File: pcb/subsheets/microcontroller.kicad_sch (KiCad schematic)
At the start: 2 parts, among them SW1 RESET, U1 Raspberry-Pi-Pico

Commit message: renamed dirs
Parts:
- renumbered SW1 to SW?
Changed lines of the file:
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@@
   (symbol (lib_id "Switch:SW_Push_Dual") (at 67.31 66.04 0) (unit 1)
     (in_bom yes) (on_board yes) (dnp no) (fields_autoplaced)
-    (property "Reference" "SW1" (at 67.31 58.42 0)
+    (property "Reference" "SW?" (at 67.31 58.42 0)
       (effects (font (size 1.27 1.27)))
     )
@@
       (project "belt"
         (path "/33e5c18d-f516-4ab7-aaea-c68685305111"
-          (reference "SW1") (unit 1)
+          (reference "SW?") (unit 1)
         )
         (path "/33e5c18d-f516-4ab7-aaea-c68685305111/0e4903ad-ca28-4f97-b4fc-99c0ae9223e0"

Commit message: fixed everything (ERC is no longer mad)
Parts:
- removed SW?: RESET, symbol Switch:SW_Push_Dual
- added SW?: RESET, symbol Switch:SW_Push_Dual
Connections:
- net +3.3V: no longer U1.35 (ADC_VREF)
- net GND: now also SW?.1, SW?.3; no longer U1.D2 (GND)
- net ~{Reset}: now also U1.37 (3V3_EN), SW?.2, SW?.4; no longer U1.30 (~{RUN})
- net SDA_{0}: now reaches U1.6 (GP_{4})
- net SCL_{0}: now reaches U1.7 (GP_{5})
- net DataBaro renamed V_{ADC0}
- net DataGndRef renamed GNDA
- net DataTemp: no longer names the net of U1.32 (GP_{27})
- no-connect marks 33 -> 25
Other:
- note added: "ADC_{2} is tied to GNDA for ADC offset approximation."
- note added: "To reduce ADC noise and offset, connect an external 3.0V shunt reference (such as LM4040) from ADC_V_{REF} to GNDA."
- note removed: "+3.3V net is otherwise unused"

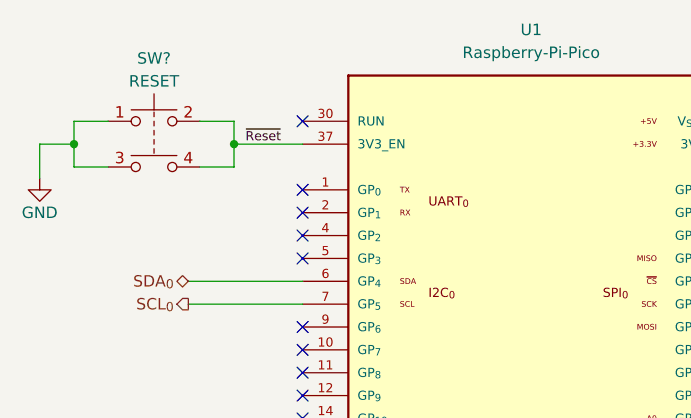
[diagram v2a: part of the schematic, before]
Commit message: fixed all the resistors
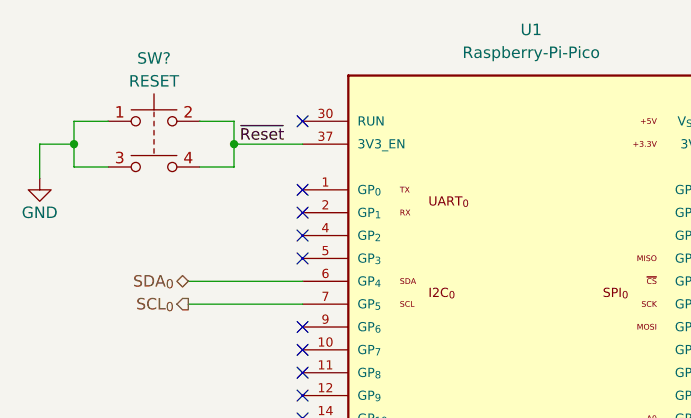
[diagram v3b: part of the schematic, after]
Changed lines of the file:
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@@
     (effects (font (size 0.635 0.635) bold) (justify left bottom))
   )
-  (label "~{Reset}" (at 90.17 71.12 0) (fields_autoplaced)
-    (effects (font (size 1.016 1.016)) (justify left bottom))
+  (label "~{Reset}" (at 89.535 71.12 0) (fields_autoplaced)
+    (effects (font (size 1.27 1.27)) (justify left bottom))
   )
   (hierarchical_label "SCL_{0}" (shape output) (at 83.82 88.9 180) (fields_autoplaced)

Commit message: mostly finished schematic
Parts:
- added D1: Power-GRN, symbol Device:LED
- added D2: Reset-RED, symbol Device:LED
- added R5, R6: 1K, symbol Device:R
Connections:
- net +3.3V: now also D2.2 (A)
- net +5V: now also D1.2 (A)
- net GND: now also R5.2, R6.2
- new net: D1.1 (K), R5.1
- new net: D2.1 (K), R6.1
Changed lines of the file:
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@@
   (title_block
     (title "BELT Microcontroller")
-    (date "2023-12-31")
+    (date "2024-01-02")
     (rev "0.2")
     (company "Rice Eclipse")
@@
     (stroke (width 0) (type default))
   )
+  (wire (pts (xy 227.33 97.79) (xy 227.33 100.33))
+    (stroke (width 0) (type default))
+  )
+  (wire (pts (xy 208.28 77.47) (xy 208.28 80.01))
+    (stroke (width 0) (type default))
+  )
   (wire (pts (xy 158.75 121.92) (xy 158.75 125.73))
     (stroke (width 0) (type default))
   )
+  (wire (pts (xy 227.33 77.47) (xy 227.33 80.01))
+    (stroke (width 0) (type default))
+  )
   (wire (pts (xy 83.82 86.36) (xy 96.52 86.36))
     (stroke (width 0) (type default))
   )
+  (wire (pts (xy 208.28 97.79) (xy 208.28 100.33))
+    (stroke (width 0) (type default))
+  )
   (wire (pts (xy 67.31 71.12) (xy 71.12 71.12))
     (stroke (width 0) (type default))
@@
     (stroke (width 0) (type default))
   )
+  (wire (pts (xy 227.33 87.63) (xy 227.33 90.17))
+    (stroke (width 0) (type default))
+  )
   (wire (pts (xy 71.12 68.58) (xy 71.12 71.12))
     (stroke (width 0) (type default))
@@
     (stroke (width 0) (type default))
   )
+  (wire (pts (xy 208.28 87.63) (xy 208.28 90.17))
+    (stroke (width 0) (type default))
+  )
   (wire (pts (xy 158.75 67.31) (xy 158.75 71.12))
     (stroke (width 0) (type default))
@@
   (wire (pts (xy 67.31 74.93) (xy 67.31 71.12))
     (stroke (width 0) (type default))
+  )
+  (text_box "Indicator LEDs"
+    (at 203.2 63.5 0) (size 39.37 44.45)
+    (stroke (width 0.254) (type solid) (color 0 0 0 1))
+    (fill (type none))
+    (effects (font (size 2.794 2.794) (thickness 0.5588) bold (color 0 0 0 1)) (justify left top))
   )
   (text "ADC_{2} is tied to GNDA for\nADC offset approximation."
@@
     (effects (font (size 1.27 1.27)) (justify left))
   )
+  (symbol (lib_id "Device:LED") (at 208.28 83.82 90) (unit 1)
+    (in_bom yes) (on_board yes) (dnp no)
+    (property "Reference" "D1" (at 210.82 82.55 90)
+      (effects (font (size 1.27 1.27)) (justify right))
+    )
+    (property "Value" "Power-GRN" (at 210.82 85.09 90)
+      (effects (font (size 1.27 1.27)) (justify right))
+    )
+    (property "Footprint" "" (at 208.28 83.82 0)
+      (effects (font (size 1.27 1.27)) hide)
+    )
+    (property "Datasheet" "~" (at 208.28 83.82 0)
+      (effects (font (size 1.27 1.27)) hide)
+    )
+    (pin "1")
+    (pin "2")
+    (instances
+      (project "belt"
+        (path "/33e5c18d-f516-4ab7-aaea-c68685305111"
+          (reference "D1") (unit 1)
+        )
+        (path "/33e5c18d-f516-4ab7-aaea-c68685305111/0e4903ad-ca28-4f97-b4fc-99c0ae9223e0"
+          (reference "D1") (unit 1)
+        )
+      )
+    )
+  )
+  (symbol (lib_id "Device:R") (at 227.33 93.98 0) (unit 1)
+    (in_bom yes) (on_board yes) (dnp no)
+    (property "Reference" "R6" (at 229.87 92.71 0)
+      (effects (font (size 1.27 1.27)) (justify left))
+    )
+    (property "Value" "1K" (at 229.87 95.25 0)
+      (effects (font (size 1.27 1.27)) (justify left))
+    )
+    (property "Footprint" "" (at 225.552 93.98 90)
+      (effects (font (size 1.27 1.27)) hide)
+    )
+    (property "Datasheet" "~" (at 227.33 93.98 0)
+      (effects (font (size 1.27 1.27)) hide)
+    )
+    (pin "1")
+    (pin "2")
+    (instances
+      (project "belt"
+        (path "/33e5c18d-f516-4ab7-aaea-c68685305111"
+          (reference "R6") (unit 1)
+        )
+        (path "/33e5c18d-f516-4ab7-aaea-c68685305111/0e4903ad-ca28-4f97-b4fc-99c0ae9223e0"
+          (reference "R6") (unit 1)
+        )
+      )
+    )
+  )
   (symbol (lib_id "power:GNDA") (at 154.94 110.49 0) (unit 1)
     (in_bom yes) (on_board yes) (dnp no)
@@
         (path "/33e5c18d-f516-4ab7-aaea-c68685305111/0e4903ad-ca28-4f97-b4fc-99c0ae9223e0"
           (reference "#PWR05") (unit 1)
+        )
+      )
+    )
+  )
+  (symbol (lib_id "power:GND") (at 227.33 100.33 0) (unit 1)
+    (in_bom yes) (on_board yes) (dnp no)
+    (property "Reference" "#PWR019" (at 227.33 106.68 0)
+      (effects (font (size 1.27 1.27)) hide)
+    )
+    (property "Value" "GND" (at 227.33 104.14 0)
+      (effects (font (size 1.27 1.27)))
+    )
+    (property "Footprint" "" (at 227.33 100.33 0)
+      (effects (font (size 1.27 1.27)) hide)
+    )
+    (property "Datasheet" "" (at 227.33 100.33 0)
+      (effects (font (size 1.27 1.27)) hide)
+    )
+    (pin "1")
+    (instances
+      (project "belt"
+        (path "/33e5c18d-f516-4ab7-aaea-c68685305111"
+          (reference "#PWR019") (unit 1)
+        )
+        (path "/33e5c18d-f516-4ab7-aaea-c68685305111/0e4903ad-ca28-4f97-b4fc-99c0ae9223e0"
+          (reference "#PWR019") (unit 1)
         )
       )
@@
     )
   )
+  (symbol (lib_id "power:+3.3V") (at 227.33 77.47 0) (unit 1)
+    (in_bom yes) (on_board yes) (dnp no)
+    (property "Reference" "#PWR018" (at 227.33 81.28 0)
+      (effects (font (size 1.27 1.27)) hide)
+    )
+    (property "Value" "+3.3V" (at 227.33 73.66 0)
+      (effects (font (size 1.27 1.27)))
+    )
+    (property "Footprint" "" (at 227.33 77.47 0)
+      (effects (font (size 1.27 1.27)) hide)
+    )
+    (property "Datasheet" "" (at 227.33 77.47 0)
+      (effects (font (size 1.27 1.27)) hide)
+    )
+    (pin "1")
+    (instances
+      (project "belt"
+        (path "/33e5c18d-f516-4ab7-aaea-c68685305111"
+          (reference "#PWR018") (unit 1)
+        )
+        (path "/33e5c18d-f516-4ab7-aaea-c68685305111/0e4903ad-ca28-4f97-b4fc-99c0ae9223e0"
+          (reference "#PWR018") (unit 1)
+        )
+      )
+    )
+  )
   (symbol (lib_id "Switch:SW_Push_Dual") (at 80.01 68.58 0) (unit 1)
     (in_bom yes) (on_board yes) (dnp no)
@@
         )
       )
+    )
+  )
+  (symbol (lib_id "Device:R") (at 208.28 93.98 0) (unit 1)
+    (in_bom yes) (on_board yes) (dnp no)
+    (property "Reference" "R5" (at 210.82 92.71 0)
+      (effects (font (size 1.27 1.27)) (justify left))
+    )
+    (property "Value" "1K" (at 210.82 95.25 0)
+      (effects (font (size 1.27 1.27)) (justify left))
+    )
+    (property "Footprint" "" (at 206.502 93.98 90)
+      (effects (font (size 1.27 1.27)) hide)
+    )
+    (property "Datasheet" "~" (at 208.28 93.98 0)
+      (effects (font (size 1.27 1.27)) hide)
+    )
+    (pin "1")
+    (pin "2")
+    (instances
+      (project "belt"
+        (path "/33e5c18d-f516-4ab7-aaea-c68685305111"
+          (reference "R5") (unit 1)
+        )
+        (path "/33e5c18d-f516-4ab7-aaea-c68685305111/0e4903ad-ca28-4f97-b4fc-99c0ae9223e0"
+          (reference "R5") (unit 1)
+        )
+      )
+    )
+  )
+  (symbol (lib_id "power:+5V") (at 208.28 77.47 0) (unit 1)
+    (in_bom yes) (on_board yes) (dnp no)
+    (property "Reference" "#PWR016" (at 208.28 81.28 0)
+      (effects (font (size 1.27 1.27)) hide)
+    )
+    (property "Value" "+5V" (at 208.28 73.66 0)
+      (effects (font (size 1.27 1.27)))
+    )
+    (property "Footprint" "" (at 208.28 77.47 0)
+      (effects (font (size 1.27 1.27)) hide)
+    )
+    (property "Datasheet" "" (at 208.28 77.47 0)
+      (effects (font (size 1.27 1.27)) hide)
+    )
+    (pin "1")
+    (instances
+      (project "belt"
+        (path "/33e5c18d-f516-4ab7-aaea-c68685305111"
+          (reference "#PWR016") (unit 1)
+        )
+        (path "/33e5c18d-f516-4ab7-aaea-c68685305111/0e4903ad-ca28-4f97-b4fc-99c0ae9223e0"
+          (reference "#PWR016") (unit 1)
+        )
+      )
+    )
+  )
+  (symbol (lib_id "power:GND") (at 208.28 100.33 0) (unit 1)
+    (in_bom yes) (on_board yes) (dnp no)
+    (property "Reference" "#PWR017" (at 208.28 106.68 0)
+      (effects (font (size 1.27 1.27)) hide)
+    )
+    (property "Value" "GND" (at 208.28 104.14 0)
+      (effects (font (size 1.27 1.27)))
+    )
+    (property "Footprint" "" (at 208.28 100.33 0)
+      (effects (font (size 1.27 1.27)) hide)
+    )
+    (property "Datasheet" "" (at 208.28 100.33 0)
+      (effects (font (size 1.27 1.27)) hide)
+    )
+    (pin "1")
+    (instances
+      (project "belt"
+        (path "/33e5c18d-f516-4ab7-aaea-c68685305111"
+          (reference "#PWR017") (unit 1)
+        )
+        (path "/33e5c18d-f516-4ab7-aaea-c68685305111/0e4903ad-ca28-4f97-b4fc-99c0ae9223e0"
+          (reference "#PWR017") (unit 1)
+        )
+      )
+    )
+  )
+  (symbol (lib_id "Device:LED") (at 227.33 83.82 90) (unit 1)
+    (in_bom yes) (on_board yes) (dnp no)
+    (property "Reference" "D2" (at 229.87 82.55 90)
+      (effects (font (size 1.27 1.27)) (justify right))
+    )
+    (property "Value" "Reset-RED" (at 229.87 85.09 90)
+      (effects (font (size 1.27 1.27)) (justify right))
+    )
+    (property "Footprint" "" (at 227.33 83.82 0)
+      (effects (font (size 1.27 1.27)) hide)
+    )
+    (property "Datasheet" "~" (at 227.33 83.82 0)
+      (effects (font (size 1.27 1.27)) hide)
+    )
+    (pin "1")
+    (pin "2")
+    (instances
+      (project "belt"
+        (path "/33e5c18d-f516-4ab7-aaea-c68685305111"
+          (reference "D2") (unit 1)
+        )
+        (path "/33e5c18d-f516-4ab7-aaea-c68685305111/0e4903ad-ca28-4f97-b4fc-99c0ae9223e0"
+          (reference "D2") (unit 1)
+        )
+      )
